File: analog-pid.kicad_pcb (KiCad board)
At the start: 2 copper layers, 39 parts, among them J1 Conn_01x06_Socket, U1 MCP6004, U2 Opamp_Dual, U3 MCP6004, U4 NC7SZ86M5X

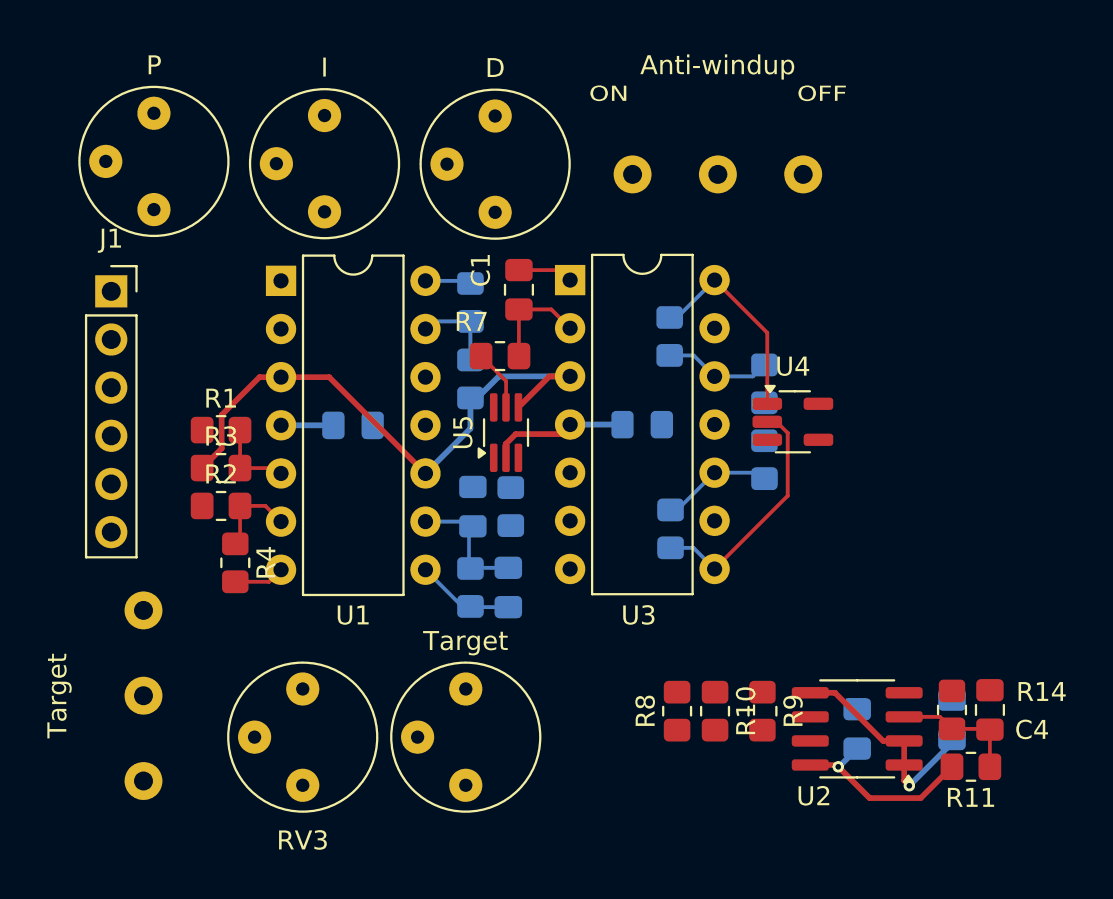
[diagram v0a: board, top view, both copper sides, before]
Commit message: Added edge cut & fixed silkscreens
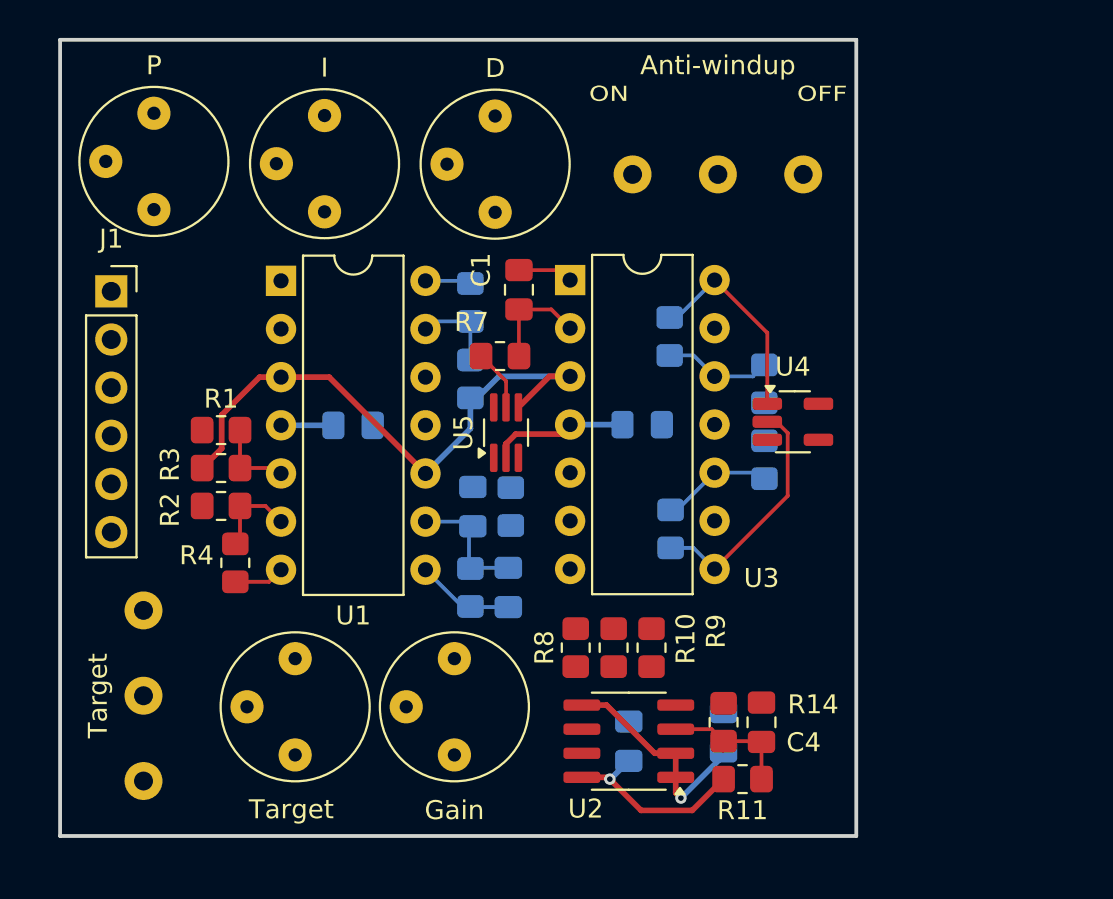
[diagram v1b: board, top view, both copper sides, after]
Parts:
- moved C4 12.1 mm to (156.8, 143.4)
- moved C5 12.1 mm to (154.8, 143.9)
- moved C8 12.1 mm to (149.8, 144.4)
- moved R11 12.1 mm to (155.8, 146.4)
- moved R14 12.1 mm to (154.8, 143.4)
- moved U2 12.1 mm to (149.8, 144.4)
- moved Target 9.14 mm to (132.2, 145.1)
- moved Gain 8.16 mm to (140.6, 145.1)
- moved R9 6.74 mm to (151.0, 139.5)
- moved R10 6.31 mm to (149.0, 139.5)
- moved R8 6.31 mm to (147.0, 139.5)
- renumbered RV3 to Gain
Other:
- board outline added: 42 x 42 mm

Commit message: Finished
Just need to double check, send to fab and order components.
Also need to test lower frequency differentiator circuit
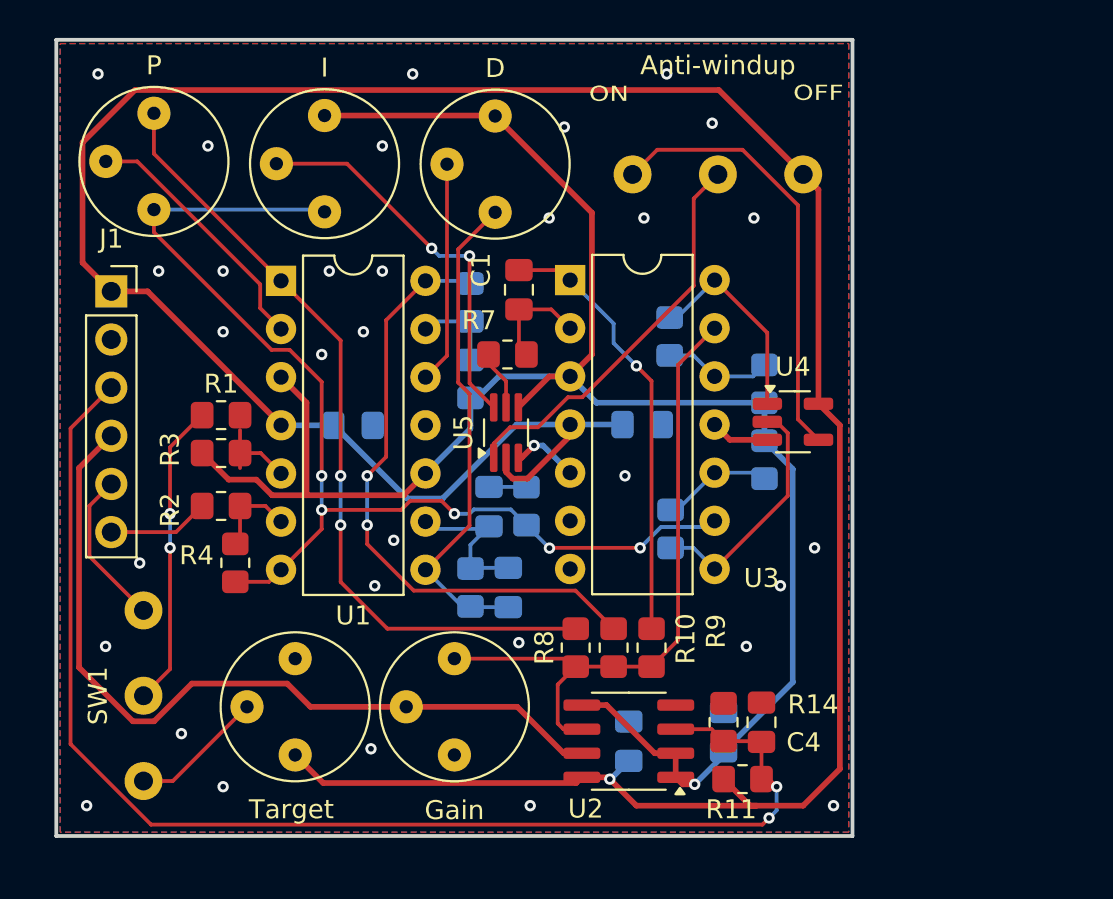
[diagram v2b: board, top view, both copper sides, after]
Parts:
- moved C3 0.85 mm to (142.4, 132.0), turned to -90 degrees
- moved R6 0.83 mm to (144.4, 132.0), turned to 90 degrees
- moved R3 0.79 mm to (128.3, 129.2)
- moved R1 0.79 mm to (128.3, 127.2)
- moved R7 0.40 mm to (143.4, 124.0)
- renumbered Target to SW1
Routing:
- net +5V: track 21.1 -> 155.2 mm
- net /Vmid_opt: track 6.77 -> 67.9 mm, vias 0 -> 2
- net /Vmid: track 43.4 -> 101.5 mm
- net /Diff: track 2.68 -> 58.7 mm, vias 0 -> 5
- net /Vout: track 0.00 -> 43.0 mm
- net /P: track 0.00 -> 42.2 mm, vias 0 -> 2
- net /V-: track 0.16 -> 34.6 mm
- net /D: track 2.43 -> 32.4 mm, vias 0 -> 2
- net Net-(SW2-C): track 0.00 -> 23.3 mm
- net /Integrator_Off: track 0.00 -> 21.2 mm
- net Net-(C2-Pad2): track 5.19 -> 26.1 mm
- net Net-(U5-NO): track 0.00 -> 20.7 mm, vias 0 -> 2
- net /I: track 2.92 -> 23.1 mm, vias 0 -> 1
- net Net-(SW1-B): track 0.00 -> 16.1 mm, vias 0 -> 2
- net Net-(U1A--): track 0.00 -> 13.6 mm
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- added copper zone on B.Cu, net GND
- added copper zone on F.Cu, net GND
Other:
- board text added: "Analog PID Controller"
- board text added: "MANUAL"
- board text added: "PIN"
- board text added: "SWITCH TARGET"

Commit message: Added pin designators. **Need to add testpads too
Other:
- board text added: "5V"
- board text added: "GND"
- board text added: "MES"
- board text added: "MID"
- board text added: "OUT"
- board text added: "REF"
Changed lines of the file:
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@@
 		(layer "Edge.Cuts")
+	)
+	(gr_text "5V"
+		(at 120.6 120.8 90)
+		(layer "B.SilkS")
+		(effects
+			(font
+				(size 0.7 0.7)
+				(thickness 0.15)
+			)
+			(justify mirror)
+		)
 	)
 	(gr_text "PIN"
@@
 			(font
 				(size 0.8 1)
+				(thickness 0.15)
+			)
+			(justify mirror)
+		)
+	)
+	(gr_text "MES"
+		(at 120.6 133.4 90)
+		(layer "B.SilkS")
+		(effects
+			(font
+				(size 0.7 0.7)
 				(thickness 0.15)
 			)
@@
 		)
 	)
+	(gr_text "MID"
+		(at 120.6 125.8 90)
+		(layer "B.SilkS")
+		(effects
+			(font
+				(size 0.7 0.7)
+				(thickness 0.15)
+			)
+			(justify mirror)
+		)
+	)
 	(gr_text "Analog PID Controller"
 		(at 157 111.2 0)
@@
 		)
 	)
+	(gr_text "REF"
+		(at 120.6 130.8 90)
+		(layer "B.SilkS")
+		(effects
+			(font
+				(size 0.7 0.7)
+				(thickness 0.15)
+			)
+			(justify mirror)
+		)
+	)
+	(gr_text "OUT"
+		(at 120.6 128.4 90)
+		(layer "B.SilkS")
+		(effects
+			(font
+				(size 0.7 0.7)
+				(thickness 0.15)
+			)
+			(justify mirror)
+		)
+	)
+	(gr_text "GND"
+		(at 120.6 123.2 90)
+		(layer "B.SilkS")
+		(effects
+			(font
+				(size 0.7 0.7)
+				(thickness 0.15)
+			)
+			(justify mirror)
+		)
+	)

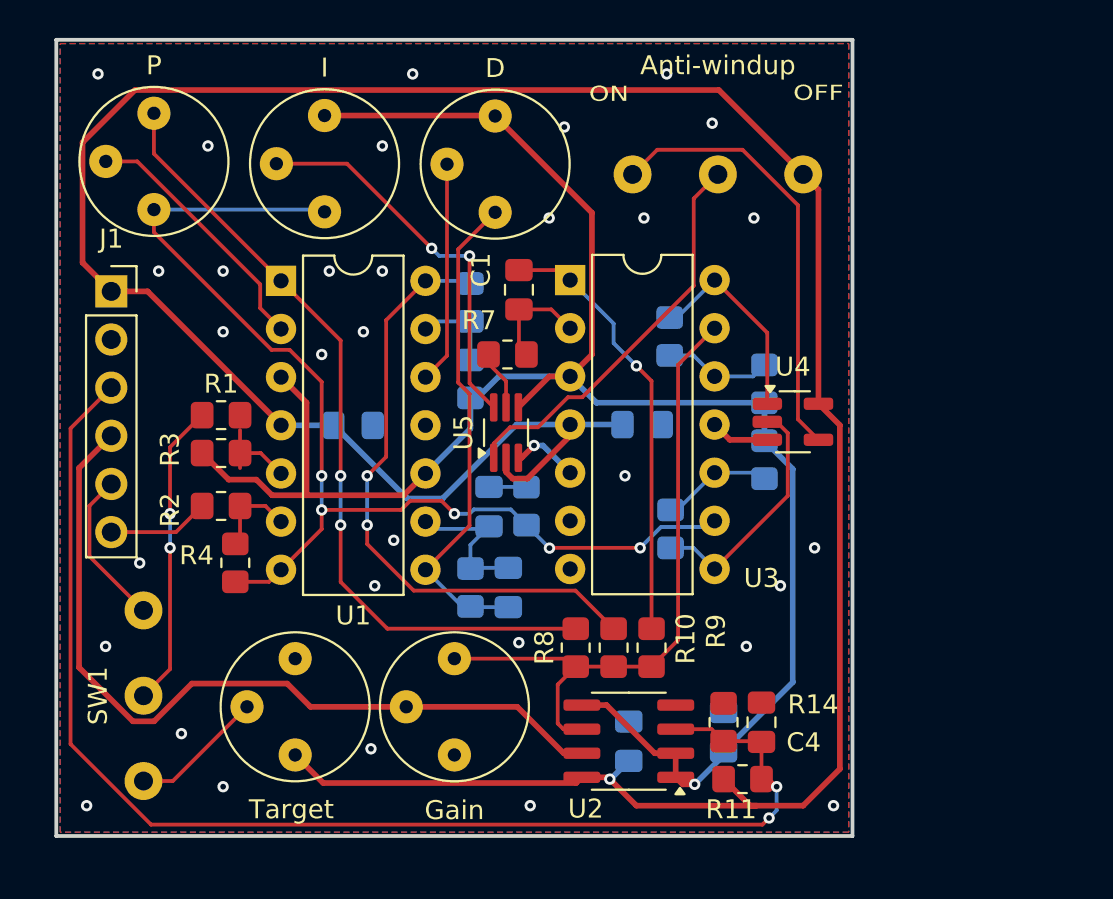
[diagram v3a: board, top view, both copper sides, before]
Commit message: Finished
Test points not needed.
Gonna skip the TVS diodes.
Finished decoupling caps.
Added rounded corners & mounting holes.
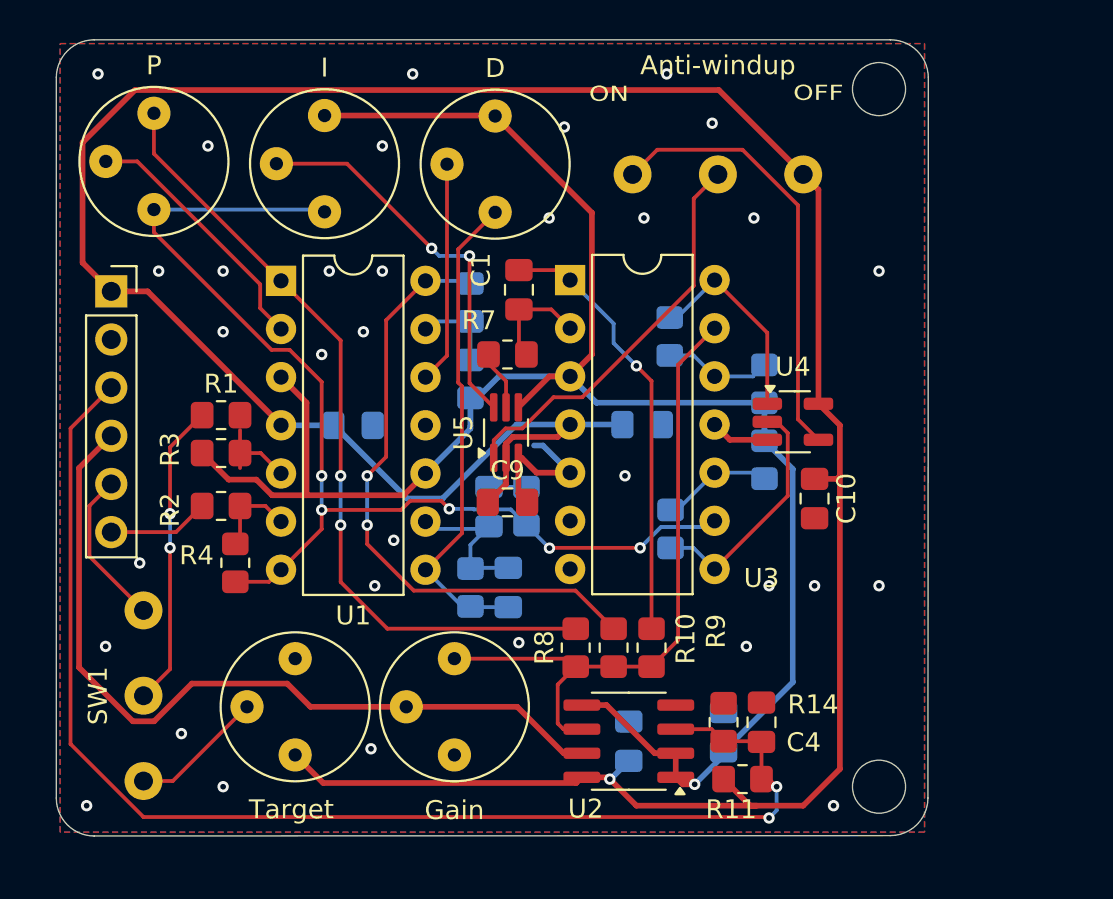
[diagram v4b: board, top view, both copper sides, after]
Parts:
- added C10: 100nF, Capacitor_SMD:C_0805_2012Metric_Pad1.18x1.45mm_HandSolder, F.Cu at (159.6, 131.6)
- added C9: 100nF, Capacitor_SMD:C_0805_2012Metric_Pad1.18x1.45mm_HandSolder, F.Cu at (143.4, 131.8)
- U2: value Opamp_Dual -> TSV792IDT
- U5: value ~ -> TS5A4624
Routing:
- net GND: track 6.71 -> 11.2 mm
- net +5V: track 155.2 -> 158.1 mm
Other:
- board size 42 x 42 mm -> 46 x 42 mm

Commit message: finished
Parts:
- C2: value 6nF -> 100pF
- C3: value 2nF -> 1.5nF
- R12: value 1Meg -> 100k
- R13: value 100 -> 10k
- R15, R18: value 5k -> 1k
- R16, R17: value 5k -> 10k
- R5: value 2k -> 1Meg
- R6: value 2k -> 10k
